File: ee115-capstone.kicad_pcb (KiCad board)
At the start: 4 copper layers, 171 parts, among them J1 2171790001, J2 9V_BATTERY, J3 Conn_01x04_Pin, J4 Conn_01x04_Pin, J5 Conn_01x03_Pin, Q1 PMOS, Q2 NMOS, Q3 NPN, Q4 AO3400A, Q5 AO3400A, Q6 NMOS, Q7 PNP, Q8 NPN, SW1 SW_Push, SW2 SW_Push, SW3 SW_Push, SW4 GF-123-0054, U1 OPA2140AIDR, U10 SN74LVC1G02DCKR (NOR), U11 SN74LVC1G02DCKR (NOR), U12 ALD1107PBL, U14 SL78L05, U15 300P14-U, U16 OPA705PA, U17 MIC4605-2YM-TR, U18 OPA705PA, U19 OPA705PA, U2 CD4052BPWR, U20 AD8038, U21 MCP6571T-E/OT, U3 LM393DR, U4 ADG601BRMZ-REEL7, U5 ESP32-C3-WROOM-02-N4, U6 AP2112K-3.3, U7 MCP601T-E_OT, U8 MCP6571T-E/OT, U9 MCP6571T-E/OT

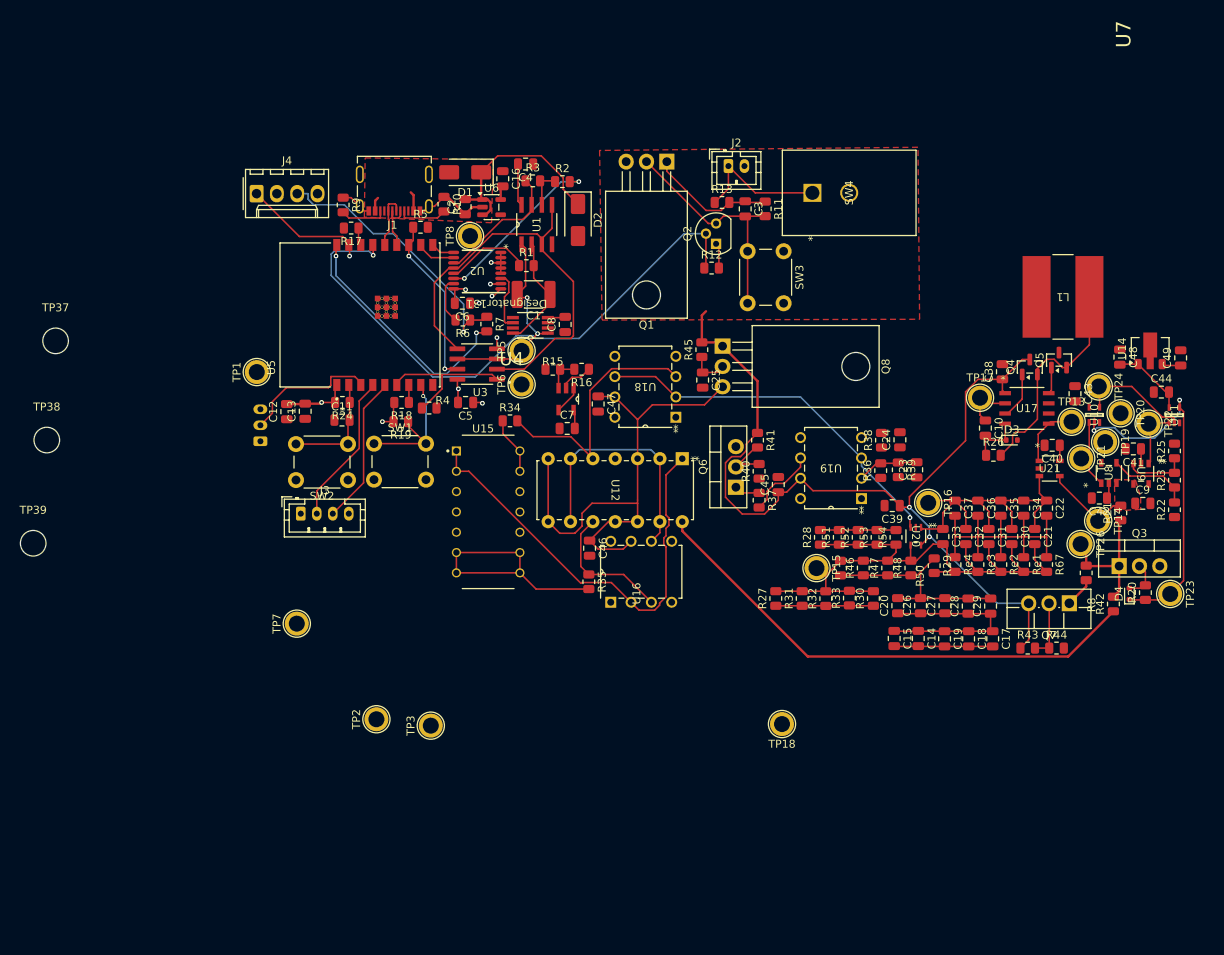
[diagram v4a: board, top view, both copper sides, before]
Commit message: Revert "init pcb"
This reverts commit 9bdb2c35d816e1c0bde8256efe77796e7b93f096.
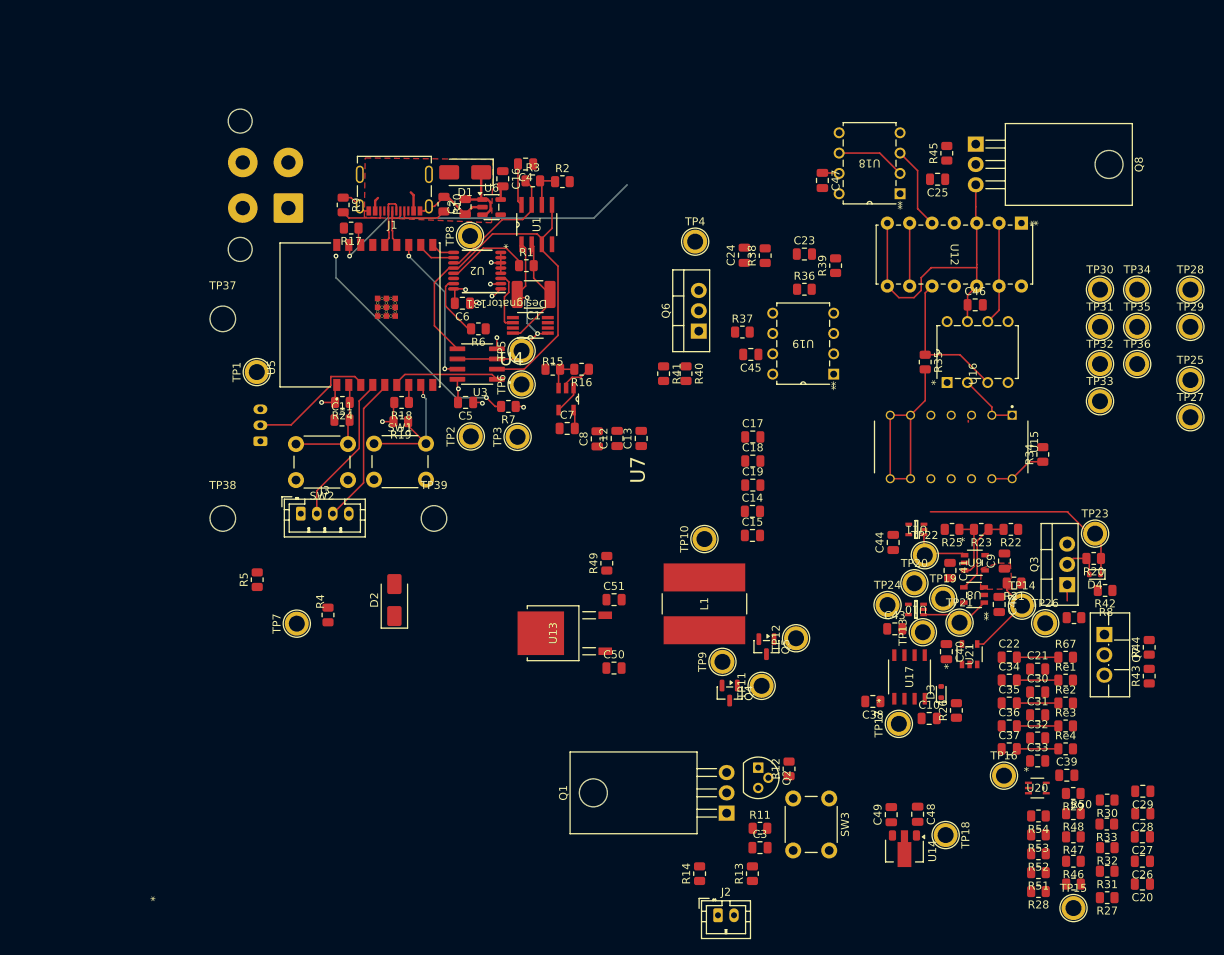
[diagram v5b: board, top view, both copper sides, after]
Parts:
- removed J4: Conn_01x04_Pin, Connector_Molex:Molex_KK-254_AE-6410-04A_1x04_P2.54mm_Vertical
- removed SW4: GF-123-0054, footprints:SW2_GF-123-0054_CWI
- added C50: C, Capacitor_SMD:C_0805_2012Metric, F.Cu at (105.3, 159.8)
- added C51: C, Capacitor_SMD:C_0805_2012Metric, F.Cu at (105.3, 151.2)
- added J6: Conn_02x02_Odd_Even, Connector_Molex:Molex_Mega-Fit_76829-0004_2x02_P5.70mm_Vertical, B.Cu at (64.6, 102.3)
- added R14: 0, Resistor_SMD:R_0805_2012Metric, F.Cu at (116.0, 185.5)
- added R49: 0, Resistor_SMD:R_0805_2012Metric, F.Cu at (104.4, 146.7)
- added TP10: TestPoint, TestPoint:TestPoint_Plated_Hole_D2.0mm, F.Cu at (116.6, 143.7)
- added TP11: TestPoint, TestPoint:TestPoint_Plated_Hole_D2.0mm, F.Cu at (123.8, 162.0)
- added TP12: TestPoint, TestPoint:TestPoint_Plated_Hole_D2.0mm, F.Cu at (128.1, 156.1)
- added TP25: TestPoint, TestPoint:TestPoint_Plated_Hole_D2.0mm, F.Cu at (177.3, 123.8)
- added TP27: TestPoint, TestPoint:TestPoint_Plated_Hole_D2.0mm, F.Cu at (177.3, 128.4)
- added TP28: TestPoint, TestPoint:TestPoint_Plated_Hole_D2.0mm, F.Cu at (177.3, 112.5)
- added TP29: TestPoint, TestPoint:TestPoint_Plated_Hole_D2.0mm, F.Cu at (177.3, 117.2)
- added TP30: TestPoint, TestPoint:TestPoint_Plated_Hole_D2.0mm, F.Cu at (166.1, 112.5)
- added TP31: TestPoint, TestPoint:TestPoint_Plated_Hole_D2.0mm, F.Cu at (166.1, 117.2)
- added TP32: TestPoint, TestPoint:TestPoint_Plated_Hole_D2.0mm, F.Cu at (166.1, 121.8)
- added TP33: TestPoint, TestPoint:TestPoint_Plated_Hole_D2.0mm, F.Cu at (166.1, 126.5)
- added TP34: TestPoint, TestPoint:TestPoint_Plated_Hole_D2.0mm, F.Cu at (170.7, 112.5)
- added TP35: TestPoint, TestPoint:TestPoint_Plated_Hole_D2.0mm, F.Cu at (170.7, 117.2)
- added TP36: TestPoint, TestPoint:TestPoint_Plated_Hole_D2.0mm, F.Cu at (170.7, 121.8)
- added TP4: TestPoint, TestPoint:TestPoint_Plated_Hole_D2.0mm, F.Cu at (115.4, 106.5)
- added TP9: TestPoint, TestPoint:TestPoint_Plated_Hole_D2.0mm, F.Cu at (118.9, 159.0)
- added U13: LD39150DT33-R, footprints_pretty:SOT_0DT33-R_STM, F.Cu at (97.7, 155.4)
- moved J2 93.7 mm to (118.3, 190.7)
- moved R13 84.0 mm to (122.6, 185.5), turned to 90 degrees
- moved Q1 81.8 mm to (119.4, 177.9), turned to 90 degrees
- moved C3 79.9 mm to (123.5, 182.2), turned to 0 degrees
- moved R11 77.4 mm to (123.5, 179.8), turned to 0 degrees
- moved U14 69.9 mm to (141.6, 182.7), turned to -90 degrees
- moved SW3 68.6 mm to (132.2, 176.1)
- moved C49 67.6 mm to (140.0, 178.1)
- moved R34 66.7 mm to (158.9, 133.1), turned to 90 degrees
- moved Q2 65.7 mm to (123.3, 172.2), turned to -90 degrees
- moved R12 63.3 mm to (127.2, 172.4), turned to 90 degrees
- moved C48 62.5 mm to (143.3, 178.1)
- moved L1 59.0 mm to (116.6, 151.8), turned to 90 degrees
- moved U15 58.4 mm to (147.4, 132.2), turned to -90 degrees
- moved C46 57.0 mm to (150.4, 114.4), turned to 0 degrees
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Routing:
- net +9V: track 134.2 -> 0.00 mm, vias 2 -> 0
- net Net-(U20--): track 78.8 -> 0.00 mm
- net /POWER_LATCH: track 73.8 -> 0.00 mm, vias 1 -> 0
- net /Buck Converter/I_PTAT: track 63.9 -> 0.00 mm
- net /bandgap/minus: track 55.5 -> 7.89 mm
- net /Buck Converter/error: track 41.9 -> 0.00 mm
- net +3.5V: track 38.4 -> 0.00 mm
- net GND: track 64.9 -> 26.8 mm
- net /Buck Converter/bg_volt: track 46.3 -> 8.67 mm, vias 1 -> 0
- net /Thermopile: track 34.5 -> 1.03 mm
- net Net-(Q1-G): track 29.4 -> 0.00 mm
- net /Buck Converter/switch_node: track 28.0 -> 0.00 mm
- net Net-(C20-Pad2): track 27.5 -> 0.00 mm
- net /bandgap/pwr_bus: track 66.4 -> 41.7 mm
- net /Thermistor: track 15.8 -> 39.8 mm
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- removed copper zone on F.Cu, net +9V
- removed copper zone on In1.Cu, net GND

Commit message: pcb layout draft
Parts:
- removed J6: Conn_02x02_Odd_Even, Connector_Molex:Molex_Mega-Fit_76829-0004_2x02_P5.70mm_Vertical
- removed TP20: TestPoint, TestPoint:TestPoint_Plated_Hole_D2.0mm
- added J4: Conn_01x04_Pin, Connector_Molex:Molex_KK-254_AE-6410-04A_1x04_P2.54mm_Vertical, B.Cu at (64.6, 100.4)
- added SW4: GF-123-0054, footprints_pretty:SW2_GF-123-0054_CWI, F.Cu at (114.8, 100.2)
- C1: footprint Capacitor_SMD:C_1812_4532Metric -> footprints_pretty:0805_cap_nosilk
- C10, C11, C12, C13, C14, C15, C16, C17, C18, C19, C2, C20, C21, C22, C23, C24, C25, C26, C27, C28, C29, C3, C30, C31, C32, C33, C34, C35, C36, C37, C38, C39, C4, C40, C41, C42, C43, C44, C45, C46, C47, C48, C49, C5, C50, C51, C6, C7, C8, C9: footprint Capacitor_SMD:C_0805_2012Metric -> footprints_pretty:0805_cap_nosilk
- R1, R10, R11, R12, R13, R15, R16, R17, R18, R19, R2, R20, R21, R22, R23, R24, R25, R26, R27, R28, R29, R3, R30, R31, R32, R33, R34, R35, R36, R37, R38, R39, R4, R40, R41, R42, R43, R44, R45, R46, R47, R48, R49, R5, R50, R51, R52, R53, R54, R6, R67, R7, R8, R9, Re1, Re2, Re3, Re4: footprint Resistor_SMD:R_0805_2012Metric -> footprints_pretty:res_0805_nosilk
- TP13: footprint TestPoint:TestPoint_Plated_Hole_D2.0mm -> TestPoint:TestPoint_Pad_D1.0mm
- moved TP28 92.1 mm to (126.7, 189.4)
- moved D2 62.3 mm to (106.7, 96.0), turned to 0 degrees
- moved TP27 59.5 mm to (118.4, 120.7)
- moved TP15 53.0 mm to (132.3, 146.5), turned to -90 degrees
- moved R27 50.4 mm to (133.4, 150.8), turned to 90 degrees
- moved R28 49.7 mm to (134.9, 143.9), turned to 90 degrees
- moved C20 48.7 mm to (135.1, 154.3), turned to 90 degrees
- moved R50 48.1 mm to (135.1, 147.4), turned to 90 degrees
- moved U18 47.4 mm to (125.6, 139.7), turned to -90 degrees
- moved R51 46.5 mm to (137.3, 143.9), turned to 90 degrees
- moved R31 45.8 mm to (136.7, 150.8), turned to 90 degrees
- moved C26 44.7 mm to (137.9, 154.3), turned to 90 degrees
- moved TP23 44.4 mm to (164.1, 187.4), turned to -90 degrees
- moved R46 44.2 mm to (137.9, 147.4), turned to 90 degrees
- moved R52 43.3 mm to (139.6, 143.9), turned to 90 degrees
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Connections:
- C12 pad 2: 3V3 -> +3V3
- C13 pad 2: 3V3 -> +3V3
- J3 pad 1: 3V3 -> +3V3
- R17 pad 2: 3V3 -> +3V3
- R18 pad 2: 3V3 -> +3V3
- R19 pad 2: 3V3 -> +3V3
- R24 pad 2: 3V3 -> +3V3
- TP35 pad 1: /Buck Converter/bg_volt -> /V_BG
- U18 pad 2: /Buck Converter/bg_volt -> /V_BG
- U18 pad 6: /Buck Converter/bg_volt -> /V_BG
- U19 pad 3: /Buck Converter/bg_volt -> /V_BG
- U20 pad 3: /Buck Converter/bg_volt -> /V_BG
- U5 pad 1: 3V3 -> +3V3
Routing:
- net +3V3: track 17.3 -> 289.7 mm, vias 3 -> 18
- net +9V: track 0.00 -> 255.7 mm
- net /V_BG: track 0.00 -> 126.0 mm, vias 0 -> 4
- net /Buck Converter/I_PTAT: track 0.00 -> 112.8 mm
- net /POWER_LATCH: track 0.00 -> 90.1 mm, vias 0 -> 8
- net /ADC-MCU/ESP_ADC_1: track 30.0 -> 117.6 mm
- net Net-(U20--): track 0.00 -> 74.5 mm
- net +3.5V: track 0.00 -> 70.7 mm
- net +5V: track 4.24 -> 67.6 mm, vias 0 -> 2
- net /ADC-MCU/COMP_OUT_BAR: track 18.9 -> 76.5 mm, vias 2 -> 8
- net /Buck Converter/error: track 0.00 -> 54.6 mm
- net /bandgap/vref: track 10.4 -> 61.2 mm, vias 0 -> 5
- net /Thermopile: track 1.03 -> 49.8 mm, vias 1 -> 8
- net /Buck Converter/switch_node: track 0.00 -> 39.7 mm
- net /ADC-MCU/COMP_OUT: track 13.5 -> 48.3 mm, vias 0 -> 2
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- added copper zone on B.Cu, net GND
- added copper zone on F.Cu, net GND
- removed copper zone on F.Cu, net /Buck Converter/Sawtooth Generator/saw
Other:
- board outline added: 115.8 x 98.2 mm
- board text added: "By: Liam Swist Matthew Tsai Solamon Ta Steve Briones"

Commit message: another draft
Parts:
- removed TP17: TestPoint, TestPoint:TestPoint_Plated_Hole_D2.0mm
- TP11: footprint TestPoint:TestPoint_Plated_Hole_D2.0mm -> TestPoint:TestPoint_Pad_D1.0mm
- moved R26 7.58 mm to (133.1, 163.0)
- moved C10 6.64 mm to (130.2, 165.9)
- moved D3 5.78 mm to (132.7, 166.7), turned to -90 degrees
- moved U17 4.40 mm to (129.3, 161.2)
- moved C38 4.25 mm to (124.8, 164.6)
- moved TP11 4.10 mm to (125.5, 162.6)
- moved Q4 3.65 mm to (121.1, 163.7)
- moved TP12 0.67 mm to (125.5, 156.2)
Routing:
- net /Buck Converter/high: track 17.0 -> 8.79 mm
- net +9V: track 255.7 -> 261.2 mm
- net /Buck Converter/switch_node: track 39.7 -> 34.5 mm
- net /Buck Converter/low: track 9.67 -> 5.25 mm
- net /Buck Converter/pwm: track 6.63 -> 10.9 mm
- net Net-(D3-K): track 11.3 -> 7.62 mm
- net Net-(U17-HB): track 0.00 -> 2.18 mm

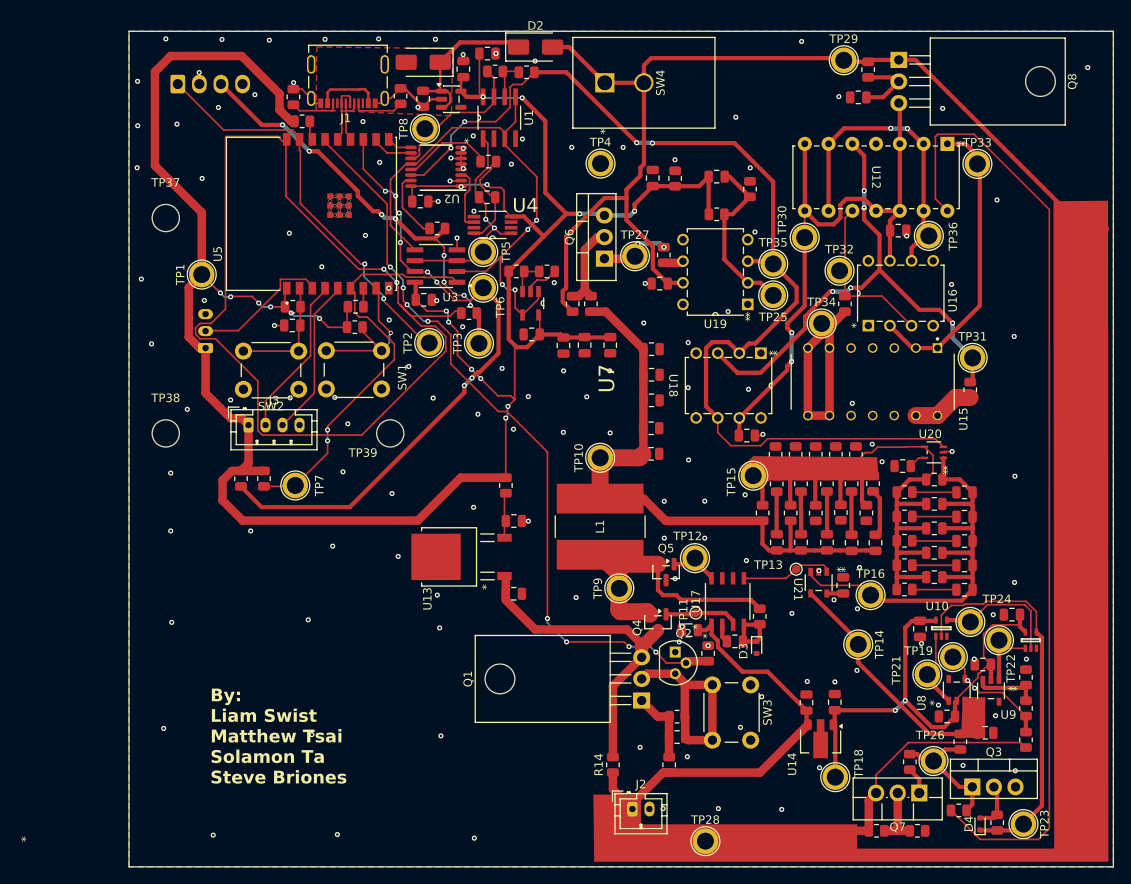
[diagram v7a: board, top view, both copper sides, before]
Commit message: fixed drc errors
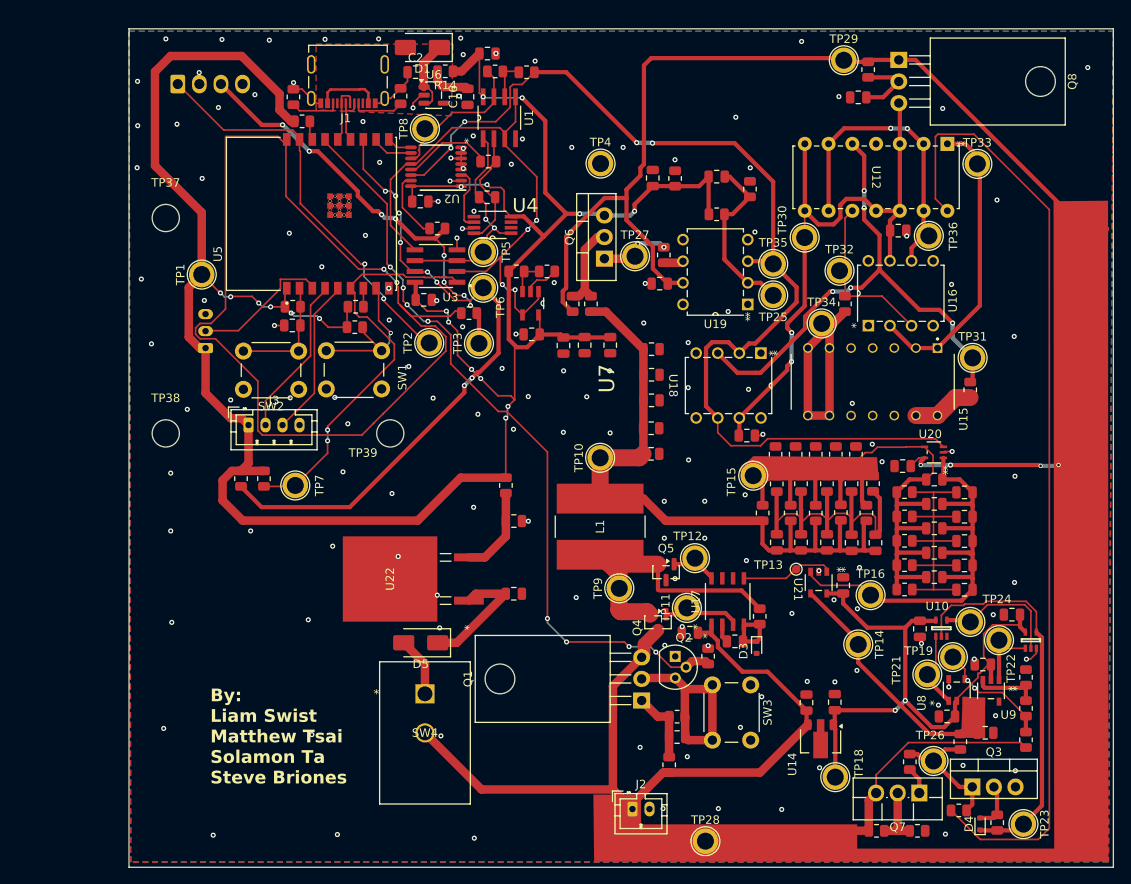
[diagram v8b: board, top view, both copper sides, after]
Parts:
- removed D2: SS14, Diode_SMD:D_SMA
- removed U13: LD39150DT33-R, footprints_pretty:SOT_0DT33-R_STM
- added D5: SS14, Diode_SMD:D_SMA, F.Cu at (93.2, 166.1)
- added U22: NCP565D2T33R4G, footprints:D2PAK3_ONS, F.Cu at (89.6, 158.6)
- C16, C2: footprint footprints_pretty:0805_cap_nosilk -> Capacitor_SMD:C_0805_2012Metric
- SW4: footprint footprints_pretty:SW2_GF-123-0054_CWI -> footprints:SW2_GF-123-0054_CWI
- TP11: footprint TestPoint:TestPoint_Pad_D1.0mm -> TestPoint:TestPoint_Plated_Hole_D2.0mm
- moved R14 83.9 mm to (96.1, 98.9), turned to 180 degrees
- moved SW4 74.9 mm to (93.7, 172.1), turned to 0 degrees
- moved C16 3.30 mm to (98.7, 101.9), turned to 90 degrees
- moved C2 3.26 mm to (92.6, 99.0), turned to 0 degrees
- moved U6 2.11 mm to (94.7, 101.7)
- moved D1 1.74 mm to (93.4, 96.1)
- moved TP11 1.21 mm to (124.5, 162.0)
- moved Q2 0.50 mm to (123.1, 167.7)
- moved R12 0.34 mm to (127.0, 167.7)
- moved C38 0.30 mm to (124.8, 164.9)
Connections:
- C16 pad 2: +3V3 -> Net-(U6-VOUT)
- C50 pad 1: +9V -> Net-(D5-K)
- R14 pad 1: +9V -> +3V3
- R14 pad 2: +9V -> Net-(U6-VOUT)
- U6 pad 5: +3V3 -> Net-(U6-VOUT)
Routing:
- net Net-(C20-Pad2): track 25.8 -> 53.3 mm
- net GND: track 28.8 -> 46.3 mm, vias 141 -> 146
- net +9V: track 261.2 -> 278.4 mm, vias 0 -> 4
- net Net-(D5-K): track 0.00 -> 15.1 mm
- net Net-(C22-Pad2): track 25.9 -> 37.4 mm
- net Net-(D1-K): track 19.4 -> 8.71 mm
- net +3.5V: track 70.7 -> 81.0 mm
- net +5V: track 67.6 -> 77.3 mm
- net Net-(U22-VOUT): track 5.30 -> 10.7 mm
- net Net-(U6-VOUT): track 0.00 -> 5.05 mm
- net Net-(U1-INA-): track 11.7 -> 14.5 mm
- net Net-(Q1-G): track 25.2 -> 24.3 mm
- net +3V3: track 289.7 -> 289.0 mm
- net /POWER_LATCH: track 90.1 -> 90.7 mm
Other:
- board size 115.8 x 98.2 mm -> 115.8 x 98.6 mm
